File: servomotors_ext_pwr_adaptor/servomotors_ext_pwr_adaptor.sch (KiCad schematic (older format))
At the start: 1 part

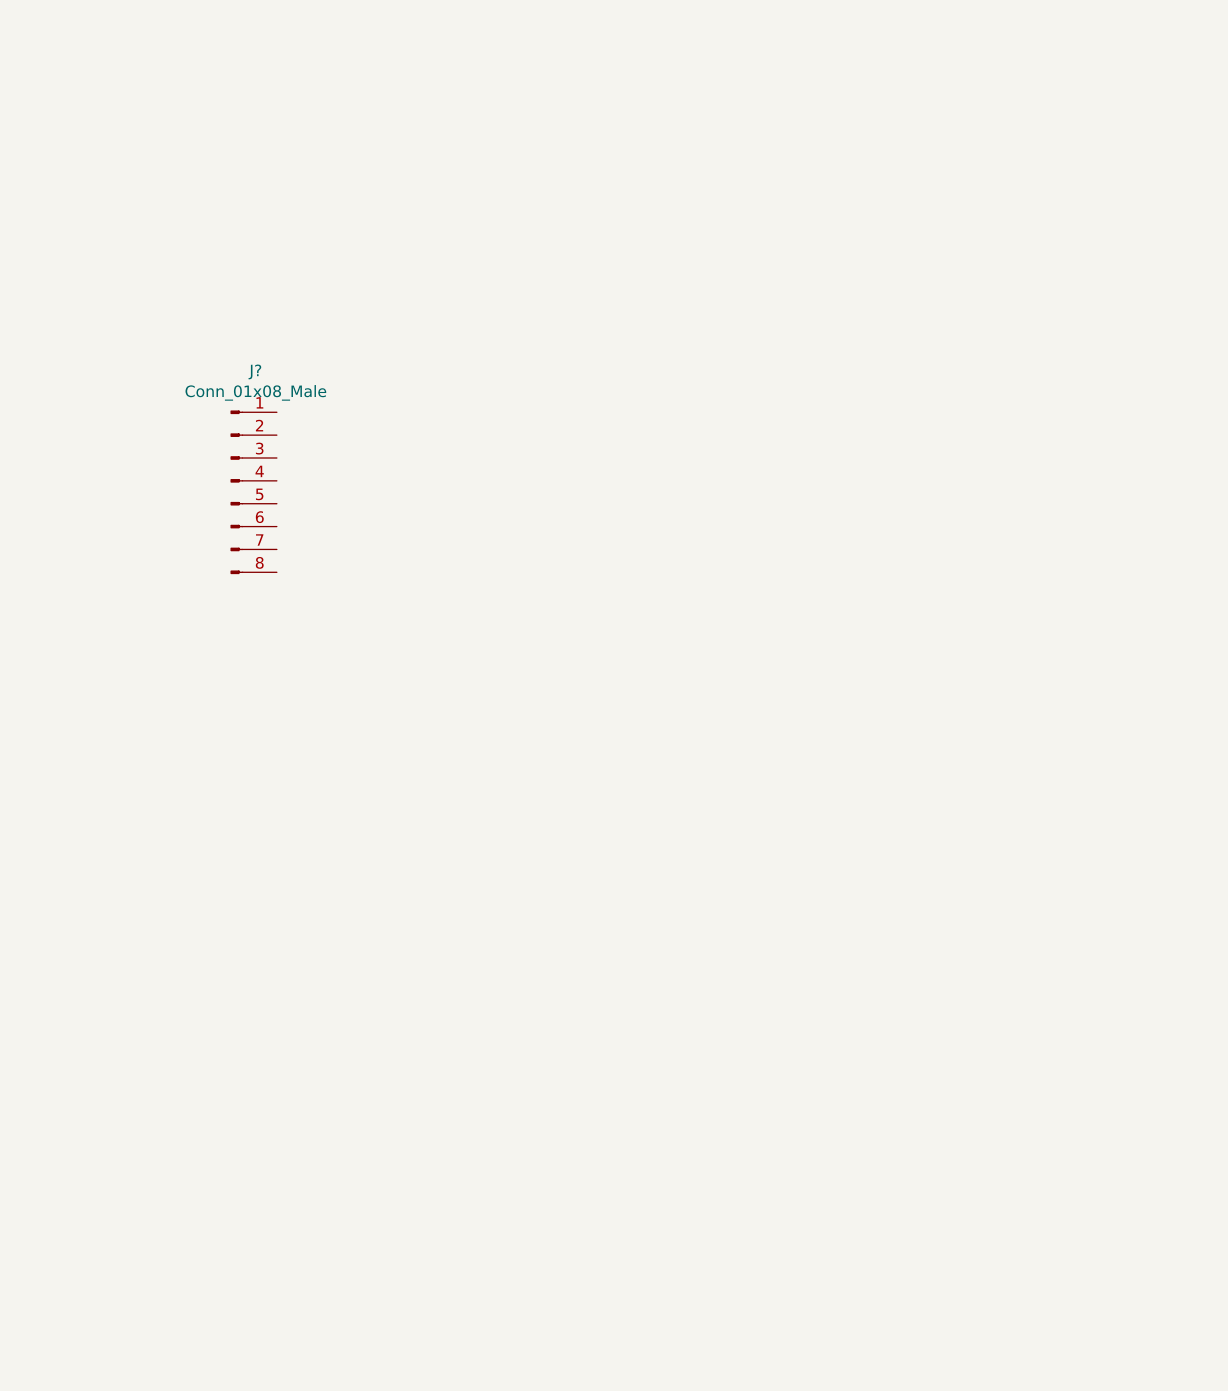
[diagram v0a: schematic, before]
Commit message: Schematic done. Symbols and footrpints added
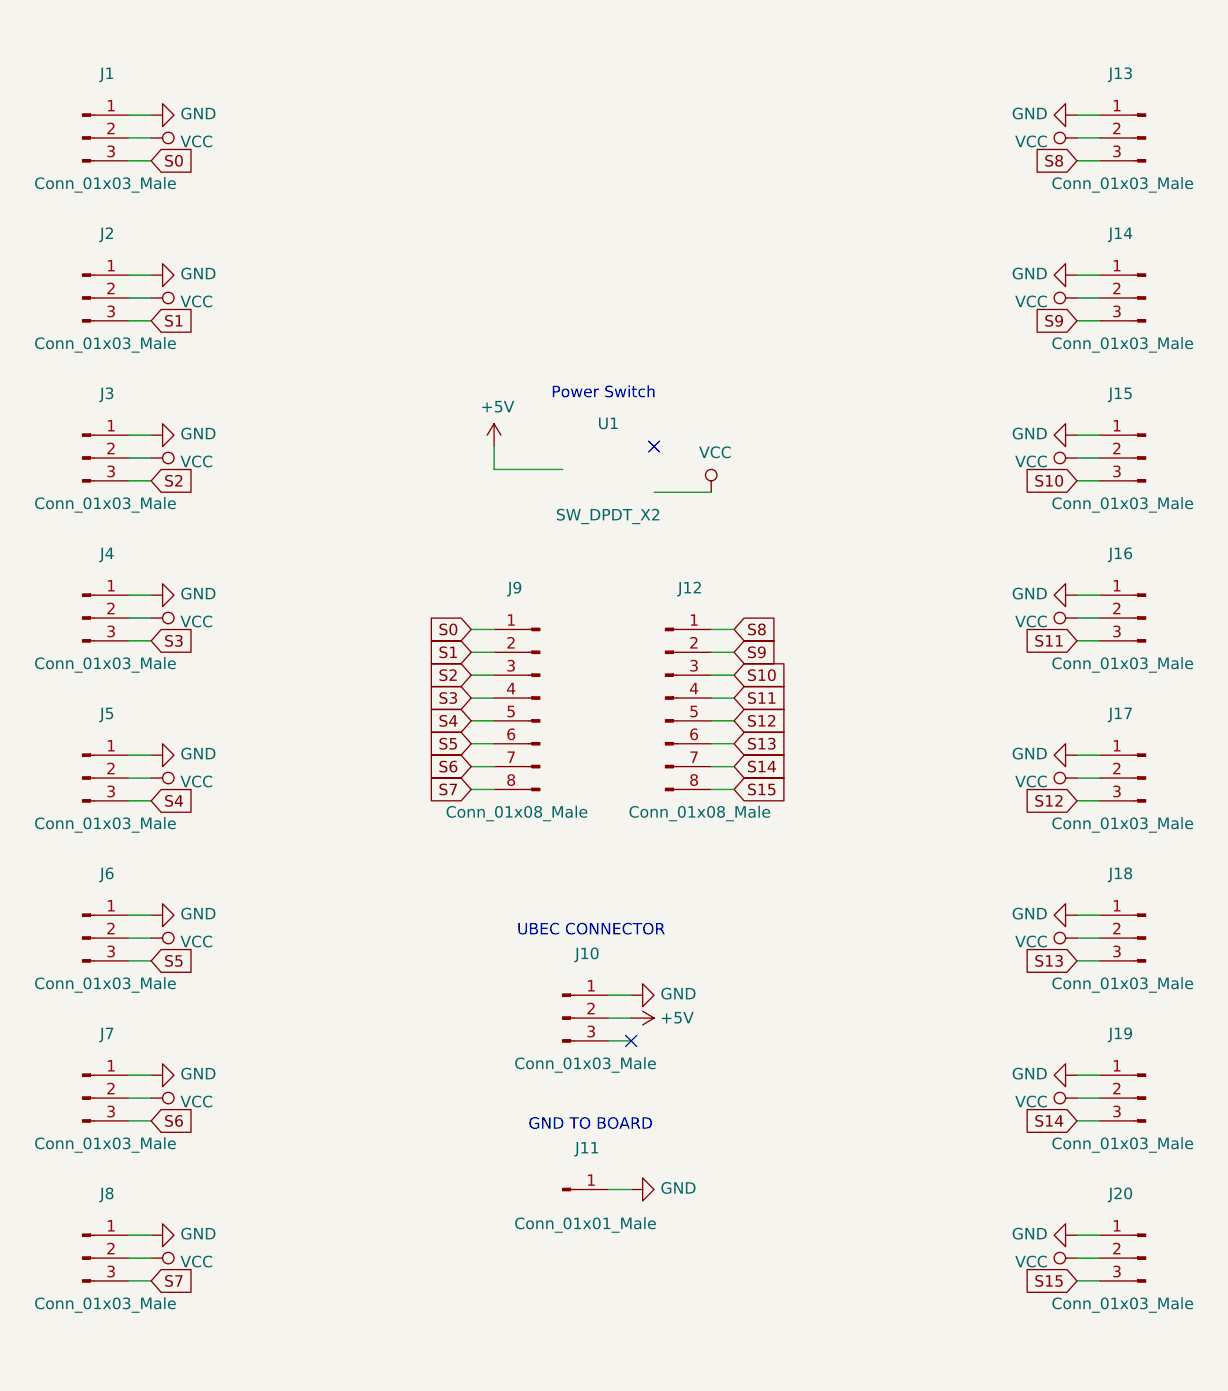
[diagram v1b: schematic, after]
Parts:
- added J1, J10, J13, J14, J15, J16, J17, J18, J19, J2, J20, J3, J4, J5, J6, J7, J8: Conn_01x03_Male, Connector_PinHeader_2.54mm:PinHeader_1x03_P2.54mm_Vertical, symbol Connector:Conn_01x03_Male
- added J11: Conn_01x01_Male, Connector_PinHeader_2.54mm:PinHeader_1x03_P2.54mm_Vertical, symbol Connector:Conn_01x01_Male
- added J12: Conn_01x08_Male, Connector_PinHeader_2.54mm:PinHeader_1x08_P2.54mm_Vertical, symbol Connector:Conn_01x08_Male
- added U1: SW_DPDT_X2, kicad-jcarolinares:Switch_Slide_11.6x4mm_EG1218, symbol kicad-jcarolinares:SW_DPDT_X2
- J9: renamed from J?; footprint (none) -> Connector_PinHeader_2.54mm:PinHeader_1x08_P2.54mm_Vertical
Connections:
- net S0: now reaches J9.1 (Pin_1)
- net S0: now also J1.3 (Pin_3)
- net S1: now reaches J9.2 (Pin_2)
- net S1: now also J2.3 (Pin_3)
- net S2: now reaches J9.3 (Pin_3)
- net S2: now also J3.3 (Pin_3)
- net S3: now reaches J9.4 (Pin_4)
- net S3: now also J4.3 (Pin_3)
- net S4: now reaches J9.5 (Pin_5)
- net S4: now also J5.3 (Pin_3)
- net S5: now reaches J9.6 (Pin_6)
- net S5: now also J6.3 (Pin_3)
- net S6: now reaches J9.7 (Pin_7)
- net S6: now also J7.3 (Pin_3)
- net S7: now reaches J9.8 (Pin_8)
- net S7: now also J8.3 (Pin_3)
- new net +5V: J10.2 (Pin_2)
- new net GND: J1.1 (Pin_1), J10.1 (Pin_1), J11.1 (Pin_1), J13.1 (Pin_1), J14.1 (Pin_1), J15.1 (Pin_1), J16.1 (Pin_1), J17.1 (Pin_1), J18.1 (Pin_1), J19.1 (Pin_1), J2.1 (Pin_1), J20.1 (Pin_1), J3.1 (Pin_1), J4.1 (Pin_1), J5.1 (Pin_1), J6.1 (Pin_1), J7.1 (Pin_1), J8.1 (Pin_1)
- new net S10: J12.3 (Pin_3), J15.3 (Pin_3)
- new net S11: J12.4 (Pin_4), J16.3 (Pin_3)
- new net S12: J12.5 (Pin_5), J17.3 (Pin_3)
- new net S13: J12.6 (Pin_6), J18.3 (Pin_3)
- new net S14: J12.7 (Pin_7), J19.3 (Pin_3)
- new net S15: J12.8 (Pin_8), J20.3 (Pin_3)
- new net S8: J12.1 (Pin_1), J13.3 (Pin_3)
- new net S9: J12.2 (Pin_2), J14.3 (Pin_3)
- new net VCC: J1.2 (Pin_2), J13.2 (Pin_2), J14.2 (Pin_2), J15.2 (Pin_2), J16.2 (Pin_2), J17.2 (Pin_2), J18.2 (Pin_2), J19.2 (Pin_2), J2.2 (Pin_2), J20.2 (Pin_2), J3.2 (Pin_2), J4.2 (Pin_2), J5.2 (Pin_2), J6.2 (Pin_2), J7.2 (Pin_2), J8.2 (Pin_2)
- no-connect marks 0 -> 2
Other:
- note added: "GND TO BOARD"
- note added: "Power Switch"
- note added: "UBEC CONNECTOR"
- moved on the sheet: J9

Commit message: WIP PCB Almost done
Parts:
- J10: value Conn_01x03_Male -> UBEC Connector
- J11: value Conn_01x01_Male -> GND to Board; footprint Connector_PinHeader_2.54mm:PinHeader_1x03_P2.54mm_Vertical -> Connector_PinSocket_2.54mm:PinSocket_1x01_P2.54mm_Vertical
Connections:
- net +5V: now also U1.2 (B)
- net VCC: now also U1.3 (C)
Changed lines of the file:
@@
 P 5650 4950
 F 0 "J10" H 5758 5231 50  0000 C CNN
-F 1 "Conn_01x03_Male" H 5750 4750 50  0000 C CNN
+F 1 "UBEC Connector" H 5750 4750 50  0000 C CNN
 F 2 "Connector_PinHeader_2.54mm:PinHeader_1x03_P2.54mm_Vertical" H 5650 4950 50  0001 C CNN
 F 3 "~" H 5650 4950 50  0001 C CNN
@@
 P 5650 5700
 F 0 "J11" H 5758 5881 50  0000 C CNN
-F 1 "Conn_01x01_Male" H 5750 5550 50  0000 C CNN
-F 2 "Connector_PinHeader_2.54mm:PinHeader_1x03_P2.54mm_Vertical" H 5650 5700 50  0001 C CNN
+F 1 "GND to Board" H 5750 5550 50  0000 C CNN
+F 2 "Connector_PinSocket_2.54mm:PinSocket_1x01_P2.54mm_Vertical" H 5650 5700 50  0001 C CNN
 F 3 "~" H 5650 5700 50  0001 C CNN
 	1    5650 5700
@@
 $Comp
 L kicad-jcarolinares:SW_DPDT_X2 U1
-U 1 0 5CC9BCD2
+U 1 1 5CC9BCD2
 P 5850 2550
 F 0 "U1" H 5850 2750 50  0000 C CNN
@@
 Text Notes 5600 2250 0    50   ~ 0
 Power Switch
+$Comp
+L power:PWR_FLAG #FLG0101
+U 1 1 5CC0E303
+P 5250 1750
+F 0 "#FLG0101" H 5250 1825 50  0001 C CNN
+F 1 "PWR_FLAG" H 5250 1923 50  0000 C CNN
+F 2 "" H 5250 1750 50  0001 C CNN
+F 3 "~" H 5250 1750 50  0001 C CNN
+	1    5250 1750
+	1    0    0    -1
+$EndComp
+$Comp
+L power:+5V #PWR0101
+U 1 1 5CC0E715
+P 5250 1850
+F 0 "#PWR0101" H 5250 1700 50  0001 C CNN
+F 1 "+5V" H 5265 2023 50  0000 C CNN
+F 2 "" H 5250 1850 50  0001 C CNN
+F 3 "" H 5250 1850 50  0001 C CNN
+	1    5250 1850
+	-1   0    0    1
+$EndComp
+Wire Wire Line
+	5250 1750 5250 1850
 $EndSCHEMATC

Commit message: WIP Energy switch
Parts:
- added D?: LED, symbol Device:LED
- added R?: 1K, symbol Device:R
- added R?: 1M, symbol Device:R
- added U?: DMP3098L-7, kicad-jcarolinares:SOT95P240X110-3N, symbol kicad-jcarolinares:DMP3098L-7
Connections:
- net +5V: now also U?.3 (D)
- net VCC: now also U?.2 (S); no longer U1.3 (C)
- new net: U1.3 (C), U?.1 (G)
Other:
- moved on the sheet: U1
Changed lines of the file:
@@
 GND TO BOARD
-$Comp
-L power:+5V #PWR017
-U 1 1 5CC50F2E
-P 5350 2450
-F 0 "#PWR017" H 5350 2300 50  0001 C CNN
-F 1 "+5V" H 5365 2623 50  0000 C CNN
-F 2 "" H 5350 2450 50  0001 C CNN
-F 3 "" H 5350 2450 50  0001 C CNN
-	1    5350 2450
-	1    0    0    -1
-$EndComp
 $Comp
 L power:VCC #PWR021
 U 1 1 5CC51E70
-P 6300 2650
-F 0 "#PWR021" H 6300 2500 50  0001 C CNN
-F 1 "VCC" H 6318 2823 50  0000 C CNN
-F 2 "" H 6300 2650 50  0001 C CNN
-F 3 "" H 6300 2650 50  0001 C CNN
-	1    6300 2650
-	1    0    0    -1
+P 6000 2500
+F 0 "#PWR021" H 6000 2350 50  0001 C CNN
+F 1 "VCC" H 6018 2673 50  0000 C CNN
+F 2 "" H 6000 2500 50  0001 C CNN
+F 3 "" H 6000 2500 50  0001 C CNN
+	1    6000 2500
+	-1   0    0    1
 $EndComp
 Text GLabel 5250 3250 0    50   Input ~ 0
@@
 L kicad-jcarolinares:SW_DPDT_X2 U1
 U 1 1 5CC9BCD2
-P 5850 2550
-F 0 "U1" H 5850 2750 50  0000 C CNN
-F 1 "SW_DPDT_X2" H 5850 2350 50  0000 C CNN
-F 2 "kicad-jcarolinares:Switch_Slide_11.6x4mm_EG1218" H 5850 2783 50  0001 C CNN
-F 3 "https://www.e-switch.com/system/asset/product_line/data_sheet/119/EG.pdf" H 5850 2550 50  0001 C CNN
-	1    5850 2550
-	1    0    0    -1
-$EndComp
-Wire Wire Line
-	5350 2450 5350 2550
-Wire Wire Line
-	5350 2550 5650 2550
-Wire Wire Line
-	6050 2650 6300 2650
-NoConn ~ 6050 2450
-$Comp
-L power:+5V #PWR019
-U 1 1 5CCA66EA
+P 5550 1550
+F 0 "U1" H 5550 1750 50  0000 C CNN
+F 1 "SW_DPDT_X2" H 5550 1350 50  0000 C CNN
+F 2 "kicad-jcarolinares:Switch_Slide_11.6x4mm_EG1218" H 5550 1783 50  0001 C CNN
+F 3 "https://www.e-switch.com/system/asset/product_line/data_sheet/119/EG.pdf" H 5550 1550 50  0001 C CNN
+	1    5550 1550
+	0    1    1    0
+$EndComp
+NoConn ~ 5650 1750
+Wire Wire Line
+	5850 4950 5950 4950
+Text Notes 5350 850  0    50   ~ 0
+Power Switch
+$Comp
+L power:PWR_FLAG #FLG0101
+U 1 1 5CC0E303
+P 4650 1050
+F 0 "#FLG0101" H 4650 1125 50  0001 C CNN
+F 1 "PWR_FLAG" H 4650 1223 50  0000 C CNN
+F 2 "" H 4650 1050 50  0001 C CNN
+F 3 "~" H 4650 1050 50  0001 C CNN
+	1    4650 1050
+	1    0    0    -1
+$EndComp
+Wire Wire Line
+	4650 1050 4650 1150
+$Comp
+L kicad-jcarolinares:DMP3098L-7 U?
+U 1 1 5CC37B62
+P 5950 2100
+F 0 "U?" H 6108 2146 50  0000 L CNN
+F 1 "DMP3098L-7" H 6108 2055 50  0000 L CNN
+F 2 "kicad-jcarolinares:SOT95P240X110-3N" H 6200 1550 50  0001 L BNN
+F 3 "https://www.diodes.com/assets/Datasheets/ds31447.pdf" H 6200 1650 50  0001 L BNN
+F 4 "SOT-23-3 Diodes Inc." H 6200 1800 50  0001 L BNN "Field6"
+F 5 "DMP3098L-7" H 6200 1900 50  0001 L BNN "Field8"
+	1    5950 2100
+	1    0    0    -1
+$EndComp
+$Comp
+L Device:R R?
+U 0 0 5CC41522
+P 7000 1150
+F 0 "R?" H 7070 1196 50  0000 L CNN
+F 1 "1K" H 7070 1105 50  0000 L CNN
+F 2 "" V 6930 1150 50  0001 C CNN
+F 3 "~" H 7000 1150 50  0001 C CNN
+	0    7000 1150
+	1    0    0    -1
+$EndComp
+$Comp
+L Device:LED D?
+U 1 1 5CC44480
+P 7000 1550
+F 0 "D?" V 7039 1433 50  0000 R CNN
+F 1 "LED" V 6948 1433 50  0000 R CNN
+F 2 "" H 7000 1550 50  0001 C CNN
+F 3 "~" H 7000 1550 50  0001 C CNN
+	1    7000 1550
+	0    -1   -1   0
+$EndComp
+Wire Wire Line
+	7000 1300 7000 1400
+Wire Wire Line
+	6000 800  6000 900
+Wire Wire Line
+	6000 900  5550 900
+Wire Wire Line
+	5550 900  5550 1350
+Connection ~ 6000 900
+$Comp
+L Device:R R?
+U 0 0 5CC6A46A
+P 5450 2450
+F 0 "R?" H 5520 2496 50  0000 L CNN
+F 1 "1M" H 5520 2405 50  0000 L CNN
+F 2 "" V 5380 2450 50  0001 C CNN
+F 3 "~" H 5450 2450 50  0001 C CNN
+	0    5450 2450
+	1    0    0    -1
+$EndComp
+Wire Wire Line
+	5450 1750 5450 2200
+Wire Wire Line
+	5450 2200 5600 2200
+$Comp
+L power:+5V #PWR?
+U 1 1 5CC6DA7F
+P 6000 800
+F 0 "#PWR?" H 6000 650 50  0001 C CNN
+F 1 "+5V" H 6015 973 50  0000 C CNN
+F 2 "" H 6000 800 50  0001 C CNN
+F 3 "" H 6000 800 50  0001 C CNN
+	1    6000 800
+	1    0    0    -1
+$EndComp
+$Comp
+L power:+5V #PWR?
+U 1 1 5CC6EC42
+P 4650 1150
+F 0 "#PWR?" H 4650 1000 50  0001 C CNN
+F 1 "+5V" H 4665 1323 50  0000 C CNN
+F 2 "" H 4650 1150 50  0001 C CNN
+F 3 "" H 4650 1150 50  0001 C CNN
+	1    4650 1150
+	-1   0    0    1
+$EndComp
+$Comp
+L power:+5V #PWR?
+U 1 1 5CC6F505
 P 5950 4950
-F 0 "#PWR019" H 5950 4800 50  0001 C CNN
-F 1 "+5V" V 5950 5150 50  0000 C CNN
+F 0 "#PWR?" H 5950 4800 50  0001 C CNN
+F 1 "+5V" V 5965 5078 50  0000 L CNN
 F 2 "" H 5950 4950 50  0001 C CNN
 F 3 "" H 5950 4950 50  0001 C CNN
@@
 	0    1    1    0
 $EndComp
-Wire Wire Line
-	5850 4950 5950 4950
-Text Notes 5600 2250 0    50   ~ 0
-Power Switch
-$Comp
-L power:PWR_FLAG #FLG0101
-U 1 1 5CC0E303
-P 5250 1750
-F 0 "#FLG0101" H 5250 1825 50  0001 C CNN
-F 1 "PWR_FLAG" H 5250 1923 50  0000 C CNN
-F 2 "" H 5250 1750 50  0001 C CNN
-F 3 "~" H 5250 1750 50  0001 C CNN
-	1    5250 1750
-	1    0    0    -1
-$EndComp
-$Comp
-L power:+5V #PWR0101
-U 1 1 5CC0E715
-P 5250 1850
-F 0 "#PWR0101" H 5250 1700 50  0001 C CNN
-F 1 "+5V" H 5265 2023 50  0000 C CNN
-F 2 "" H 5250 1850 50  0001 C CNN
-F 3 "" H 5250 1850 50  0001 C CNN
-	1    5250 1850
-	-1   0    0    1
-$EndComp
-Wire Wire Line
-	5250 1750 5250 1850
+$Comp
+L power:GND #PWR?
+U 1 1 5CC710B6
+P 5450 2700
+F 0 "#PWR?" H 5450 2450 50  0001 C CNN
+F 1 "GND" H 5550 2550 50  0000 R CNN
+F 2 "" H 5450 2700 50  0001 C CNN
+F 3 "" H 5450 2700 50  0001 C CNN
+	1    5450 2700
+	1    0    0    -1
+$EndComp
+Wire Wire Line
+	5450 2600 5450 2700
+Wire Wire Line
+	5450 2200 5450 2300
+Connection ~ 5450 2200
+Wire Wire Line
+	6000 2400 6000 2500
+Wire Wire Line
+	6000 900  6000 1800
 $EndSCHEMATC

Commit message: PCB done. Ready for QA and Gerber files
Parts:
- removed R?: 1K, symbol Device:R
- removed R?: 1M, symbol Device:R
- added J21: 5V to VCC, Connector_PinHeader_2.54mm:PinHeader_1x02_P2.54mm_Vertical, symbol Connector:Conn_01x02_Male
- added R1: 1M, Resistor_THT:R_Axial_DIN0207_L6.3mm_D2.5mm_P7.62mm_Horizontal, symbol Device:R
- added R2: 180, Resistor_THT:R_Axial_DIN0207_L6.3mm_D2.5mm_P7.62mm_Horizontal, symbol Device:R
- D1: renamed from D?; value LED -> GREEN; footprint (none) -> LED_THT:LED_D3.0mm
- gave numbers to parts that had none: 1
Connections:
- net +5V: now also J21.1 (Pin_1)
- net GND: now also D1.1 (K), R1.2
- net VCC: now also J21.2 (Pin_2), R2.1
- net at U1.3 (C), U2.1 (G): now also R1.1
- net at D1.2 (A): now also R2.2
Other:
- note added: "5V to VCC"
- note added: "PWR LED"
- moved on the sheet: D1
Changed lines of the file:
@@
 EESchema Schematic File Version 4
 LIBS:servomotors_ext_pwr_adaptor-cache
-EELAYER 29 0
+EELAYER 26 0
 EELAYER END
 $Descr A4 11693 8268
@@
 	0    -1   1    0
 $EndComp
-Wire Wire Line
-	8000 2500 7900 2500
 $Comp
 L power:GND #PWR026
@@
 	4650 1050 4650 1150
 $Comp
-L kicad-jcarolinares:DMP3098L-7 U?
+L kicad-jcarolinares:DMP3098L-7 U2
 U 1 1 5CC37B62
 P 5950 2100
-F 0 "U?" H 6108 2146 50  0000 L CNN
-F 1 "DMP3098L-7" H 6108 2055 50  0000 L CNN
+F 0 "U2" H 5700 2250 50  0000 L CNN
+F 1 "DMP3098L-7" V 6150 1850 50  0000 L CNN
 F 2 "kicad-jcarolinares:SOT95P240X110-3N" H 6200 1550 50  0001 L BNN
 F 3 "https://www.diodes.com/assets/Datasheets/ds31447.pdf" H 6200 1650 50  0001 L BNN
@@
 $EndComp
 $Comp
-L Device:R R?
-U 0 0 5CC41522
-P 7000 1150
-F 0 "R?" H 7070 1196 50  0000 L CNN
-F 1 "1K" H 7070 1105 50  0000 L CNN
-F 2 "" V 6930 1150 50  0001 C CNN
-F 3 "~" H 7000 1150 50  0001 C CNN
-	0    7000 1150
-	1    0    0    -1
-$EndComp
-$Comp
-L Device:LED D?
+L Device:LED D1
 U 1 1 5CC44480
-P 7000 1550
-F 0 "D?" V 7039 1433 50  0000 R CNN
-F 1 "LED" V 6948 1433 50  0000 R CNN
-F 2 "" H 7000 1550 50  0001 C CNN
-F 3 "~" H 7000 1550 50  0001 C CNN
-	1    7000 1550
+P 6550 2100
+F 0 "D1" V 6589 1983 50  0000 R CNN
+F 1 "GREEN" V 6498 1983 50  0000 R CNN
+F 2 "LED_THT:LED_D3.0mm" H 6550 2100 50  0001 C CNN
+F 3 "~" H 6550 2100 50  0001 C CNN
+	1    6550 2100
 	0    -1   -1   0
 $EndComp
-Wire Wire Line
-	7000 1300 7000 1400
 Wire Wire Line
 	6000 800  6000 900
@@
 	5550 900  5550 1350
 Connection ~ 6000 900
-$Comp
-L Device:R R?
-U 0 0 5CC6A46A
-P 5450 2450
-F 0 "R?" H 5520 2496 50  0000 L CNN
-F 1 "1M" H 5520 2405 50  0000 L CNN
-F 2 "" V 5380 2450 50  0001 C CNN
-F 3 "~" H 5450 2450 50  0001 C CNN
-	0    5450 2450
-	1    0    0    -1
-$EndComp
 Wire Wire Line
 	5450 1750 5450 2200
@@
 	5450 2200 5600 2200
 $Comp
-L power:+5V #PWR?
+L power:+5V #PWR039
 U 1 1 5CC6DA7F
 P 6000 800
-F 0 "#PWR?" H 6000 650 50  0001 C CNN
+F 0 "#PWR039" H 6000 650 50  0001 C CNN
 F 1 "+5V" H 6015 973 50  0000 C CNN
 F 2 "" H 6000 800 50  0001 C CNN
@@
 $EndComp
 $Comp
-L power:+5V #PWR?
+L power:+5V #PWR017
 U 1 1 5CC6EC42
 P 4650 1150
-F 0 "#PWR?" H 4650 1000 50  0001 C CNN
+F 0 "#PWR017" H 4650 1000 50  0001 C CNN
 F 1 "+5V" H 4665 1323 50  0000 C CNN
 F 2 "" H 4650 1150 50  0001 C CNN
@@
 $EndComp
 $Comp
-L power:+5V #PWR?
+L power:+5V #PWR038
 U 1 1 5CC6F505
 P 5950 4950
-F 0 "#PWR?" H 5950 4800 50  0001 C CNN
+F 0 "#PWR038" H 5950 4800 50  0001 C CNN
 F 1 "+5V" V 5965 5078 50  0000 L CNN
 F 2 "" H 5950 4950 50  0001 C CNN
@@
 $EndComp
 $Comp
-L power:GND #PWR?
+L power:GND #PWR019
 U 1 1 5CC710B6
 P 5450 2700
-F 0 "#PWR?" H 5450 2450 50  0001 C CNN
+F 0 "#PWR019" H 5450 2450 50  0001 C CNN
 F 1 "GND" H 5550 2550 50  0000 R CNN
 F 2 "" H 5450 2700 50  0001 C CNN
@@
 $EndComp
 Wire Wire Line
-	5450 2600 5450 2700
+	6000 2400 6000 2500
+Wire Wire Line
+	6000 900  6000 1800
+$Comp
+L power:GND #PWR041
+U 1 1 5CC58EF2
+P 6550 2350
+F 0 "#PWR041" H 6550 2100 50  0001 C CNN
+F 1 "GND" H 6650 2200 50  0000 R CNN
+F 2 "" H 6550 2350 50  0001 C CNN
+F 3 "" H 6550 2350 50  0001 C CNN
+	1    6550 2350
+	1    0    0    -1
+$EndComp
+$Comp
+L power:VCC #PWR040
+U 1 1 5CC5B496
+P 6550 1450
+F 0 "#PWR040" H 6550 1300 50  0001 C CNN
+F 1 "VCC" V 6567 1578 50  0000 L CNN
+F 2 "" H 6550 1450 50  0001 C CNN
+F 3 "" H 6550 1450 50  0001 C CNN
+	1    6550 1450
+	1    0    0    -1
+$EndComp
+Text Notes 6450 2050 1    50   ~ 0
+PWR LED
+Wire Wire Line
+	7900 2500 8000 2500
+$Comp
+L Connector:Conn_01x02_Male J21
+U 1 1 5CC64734
+P 5550 6250
+F 0 "J21" H 5800 6350 50  0000 C CNN
+F 1 "5V to VCC" H 5700 6050 50  0000 C CNN
+F 2 "Connector_PinHeader_2.54mm:PinHeader_1x02_P2.54mm_Vertical" H 5550 6250 50  0001 C CNN
+F 3 "~" H 5550 6250 50  0001 C CNN
+	1    5550 6250
+	1    0    0    -1
+$EndComp
+$Comp
+L power:+5V #PWR042
+U 1 1 5CC64C16
+P 5850 6250
+F 0 "#PWR042" H 5850 6100 50  0001 C CNN
+F 1 "+5V" H 5865 6423 50  0000 C CNN
+F 2 "" H 5850 6250 50  0001 C CNN
+F 3 "" H 5850 6250 50  0001 C CNN
+	1    5850 6250
+	0    1    1    0
+$EndComp
+Wire Wire Line
+	5750 6250 5850 6250
+$Comp
+L power:VCC #PWR043
+U 1 1 5CC6740D
+P 5850 6350
+F 0 "#PWR043" H 5850 6200 50  0001 C CNN
+F 1 "VCC" V 5867 6478 50  0000 L CNN
+F 2 "" H 5850 6350 50  0001 C CNN
+F 3 "" H 5850 6350 50  0001 C CNN
+	1    5850 6350
+	0    1    1    0
+$EndComp
+Wire Wire Line
+	5750 6350 5850 6350
+Text Notes 5550 6100 0    50   ~ 0
+5V to VCC
 Wire Wire Line
 	5450 2200 5450 2300
 Connection ~ 5450 2200
 Wire Wire Line
-	6000 2400 6000 2500
-Wire Wire Line
-	6000 900  6000 1800
+	5450 2600 5450 2700
+$Comp
+L Device:R R1
+U 1 1 5CC803B0
+P 5450 2450
+F 0 "R1" H 5520 2496 50  0000 L CNN
+F 1 "1M" H 5520 2405 50  0000 L CNN
+F 2 "Resistor_THT:R_Axial_DIN0207_L6.3mm_D2.5mm_P7.62mm_Horizontal" V 5380 2450 50  0001 C CNN
+F 3 "~" H 5450 2450 50  0001 C CNN
+	1    5450 2450
+	1    0    0    -1
+$EndComp
+$Comp
+L Device:R R2
+U 1 1 5CC80428
+P 6550 1700
+F 0 "R2" H 6620 1746 50  0000 L CNN
+F 1 "180" H 6620 1655 50  0000 L CNN
+F 2 "Resistor_THT:R_Axial_DIN0207_L6.3mm_D2.5mm_P7.62mm_Horizontal" V 6480 1700 50  0001 C CNN
+F 3 "~" H 6550 1700 50  0001 C CNN
+	1    6550 1700
+	1    0    0    -1
+$EndComp
+Wire Wire Line
+	6550 1850 6550 1950
+Wire Wire Line
+	6550 1450 6550 1550
+Wire Wire Line
+	6550 2250 6550 2350
 $EndSCHEMATC
